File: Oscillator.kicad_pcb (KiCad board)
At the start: 2 copper layers, 200.9 x 113.3 mm, 228 parts, among them J201 AudioJack2, J202 AudioJack2, J203 AudioJack2, J204 Conn_01x14, J205 AudioJack2, J206 AudioJack2, J207 Conn_01x09, J208 AudioJack2, J209 AudioJack2, J210 AudioJack2, J301 Conn_01x14, J302 Conn_01x09, J303 Conn_02x05_Odd_Even, Q401 2N3904, Q402 2N3906, Q403 2N3904, Q601 Q_NJFET_DSG, Q602 Q_NJFET_DSG, Q603 2N3904, Q701 Q_NJFET_DSG, SW201 SR1712F-0204-20F0A-N9-N-027, U201 TL072, U501 TL074, U502 LM13700, U503 TL074, U601 TL074, U602 LM339, U603 TL074, U604 4066, U605 TL074, U701 OP275, U702 DMMT3904W, U703 TL072

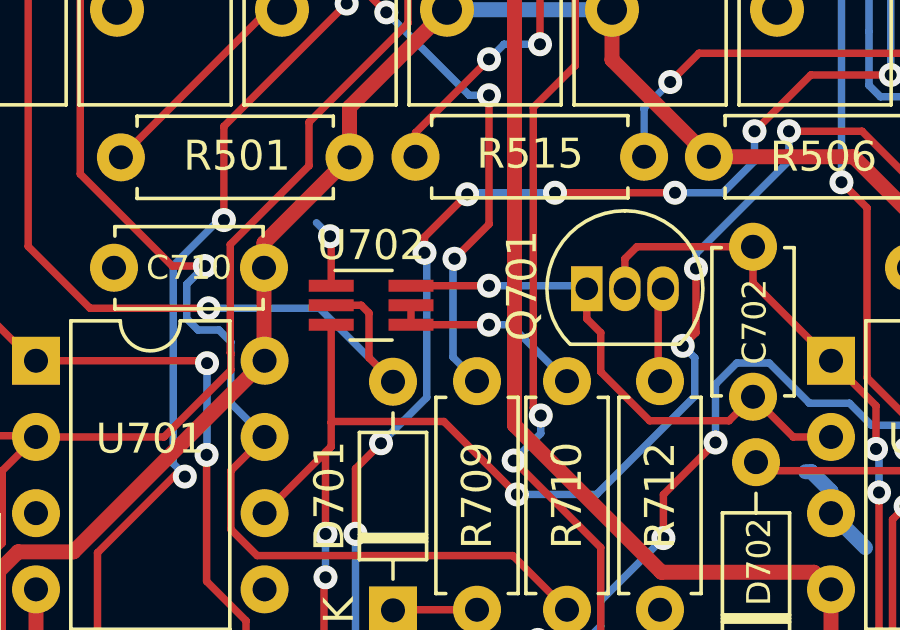
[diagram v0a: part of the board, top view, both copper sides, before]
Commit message: Moved junction away from soldering pads of U702
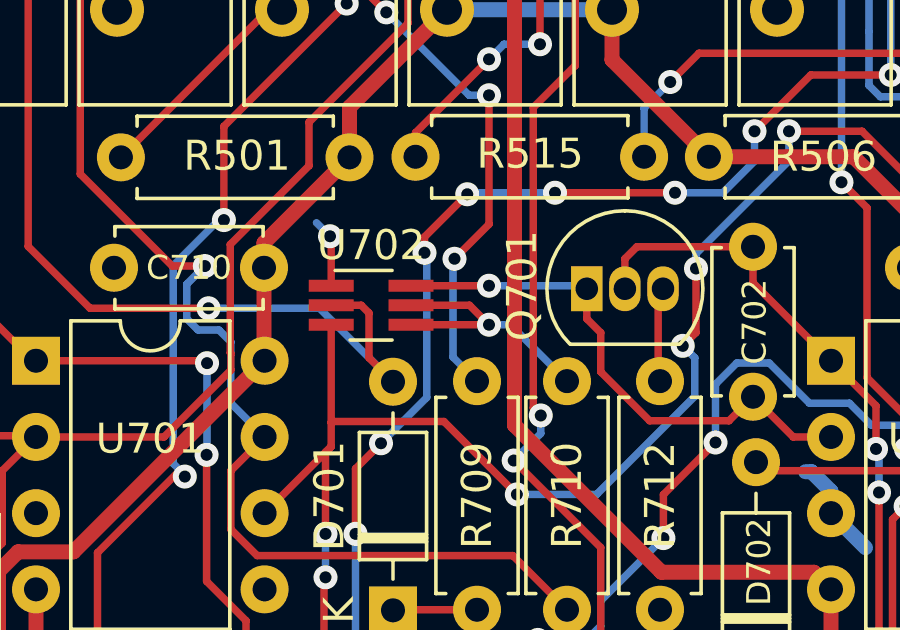
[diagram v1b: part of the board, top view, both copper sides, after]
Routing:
- net Net-(R710-Pad2): track 6.63 -> 8.85 mm
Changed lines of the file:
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@@
     (thickness 1.6)
     (drawings 53)
-    (tracks 2977)
+    (tracks 2978)
     (zones 0)
     (modules 228)
@@
   (segment (start 181.347653 45.36) (end 177.54 45.36) (width 0.25) (layer F.Cu) (net 150))
   (segment (start 183.975 47.987347) (end 181.347653 45.36) (width 0.25) (layer F.Cu) (net 150))
-  (segment (start 184.8 57.75) (end 184.8 58.4) (width 0.25) (layer F.Cu) (net 151))
   (via (at 187.400001 58.4) (size 0.8) (drill 0.4) (layers F.Cu B.Cu) (net 151))
   (segment (start 188.12 58.4) (end 187.400001 58.4) (width 0.25) (layer B.Cu) (net 151))
   (segment (start 190 60.28) (end 188.12 58.4) (width 0.25) (layer B.Cu) (net 151))
   (segment (start 187.400001 58.4) (end 184.8 58.4) (width 0.25) (layer F.Cu) (net 151))
+  (segment (start 186.750001 57.75) (end 187.400001 58.4) (width 0.25) (layer F.Cu) (net 151))
+  (segment (start 184.8 57.75) (end 186.750001 57.75) (width 0.25) (layer F.Cu) (net 151))
   (segment (start 208.6 76.28) (end 208.58 76.3) (width 0.25) (layer F.Cu) (net 152))
   (segment (start 208.6 73.3) (end 208.6 76.28) (width 0.25) (layer F.Cu) (net 152))

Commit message: Began fixing backwards op amp issue
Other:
- board text added: "oscillator / waveshaper / vca version 3 chris defrancisci"
- board text removed: "oscillator / waveshaper / vca version 2 chris defrancisci"
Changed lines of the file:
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@@
     )
   )
-  (gr_text "oscillator / waveshaper / vca\nversion 2\nchris defrancisci" (at 92.85 86.15) (layer B.SilkS)
+  (gr_text "oscillator / waveshaper / vca\nversion 3\nchris defrancisci" (at 92.85 86.15) (layer B.SilkS)
     (effects (font (size 1 1) (thickness 0.15)) (justify mirror))
   )

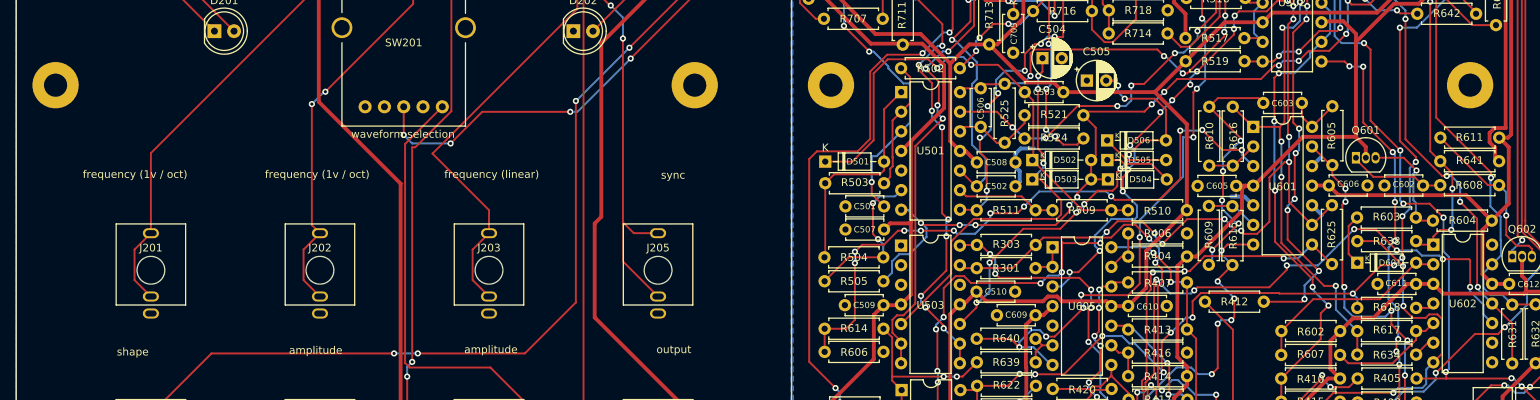
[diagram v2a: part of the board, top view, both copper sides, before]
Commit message: Fixed op amp issue
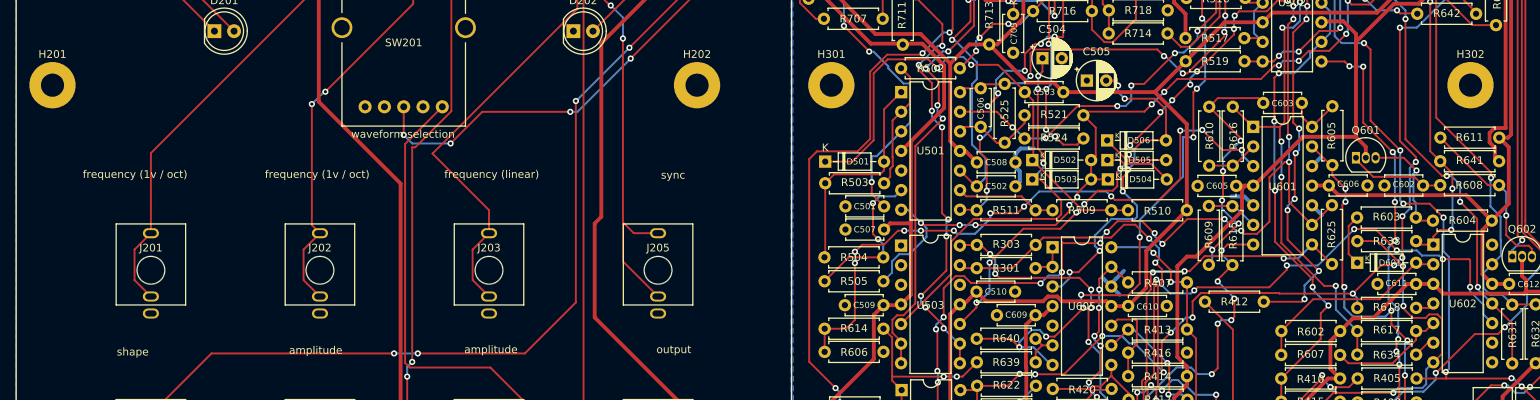
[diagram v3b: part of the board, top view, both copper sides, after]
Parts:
- removed R404: 100k, Resistor_THT:R_Axial_DIN0207_L6.3mm_D2.5mm_P7.62mm_Horizontal
- removed R406: 2k, Resistor_THT:R_Axial_DIN0207_L6.3mm_D2.5mm_P7.62mm_Horizontal
- removed REF** (x4): MountingHole_3mm_Pad, MountingHole:MountingHole_3mm_Pad
- added H201: MountingHole, MountingHole:MountingHole_3mm_Pad, F.Cu at (71.8, 83.0)
- added H202: MountingHole, MountingHole:MountingHole_3mm_Pad, F.Cu at (155.2, 83.0)
- added H301: MountingHole, MountingHole:MountingHole_3mm_Pad, F.Cu at (172.7, 83.0)
- added H302: MountingHole, MountingHole:MountingHole_3mm_Pad, F.Cu at (255.4, 83.0)
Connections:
- U605 pad 10: Net-(R413-Pad1) -> Net-(R414-Pad1)
- U605 pad 12: Net-(R401-Pad1) -> GND
- U605 pad 13: Net-(R404-Pad1) -> Net-(R401-Pad1)
- U605 pad 9: Net-(R414-Pad1) -> Net-(R413-Pad1)
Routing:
- net GND: track 20.0 -> 25.8 mm
- net Net-(R404-Pad1): track 5.74 -> 0.00 mm
- net Net-(R414-Pad1): track 5.62 -> 11.3 mm
- net Net-(R401-Pad1): track 77.7 -> 80.2 mm
- net Net-(R413-Pad1): track 16.2 -> 16.9 mm
